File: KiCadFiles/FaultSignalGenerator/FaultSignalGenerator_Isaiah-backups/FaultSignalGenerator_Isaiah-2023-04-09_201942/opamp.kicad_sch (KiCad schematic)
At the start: 16 parts, among them U10 TL074CDR, U11 TL074CDR, U12 TL074CDR, U13 TL074CDR, U5 TL074CDR, U6 TL074CDR, U7 TL074CDR, U8 TL074CDR, U9 TL074CDR

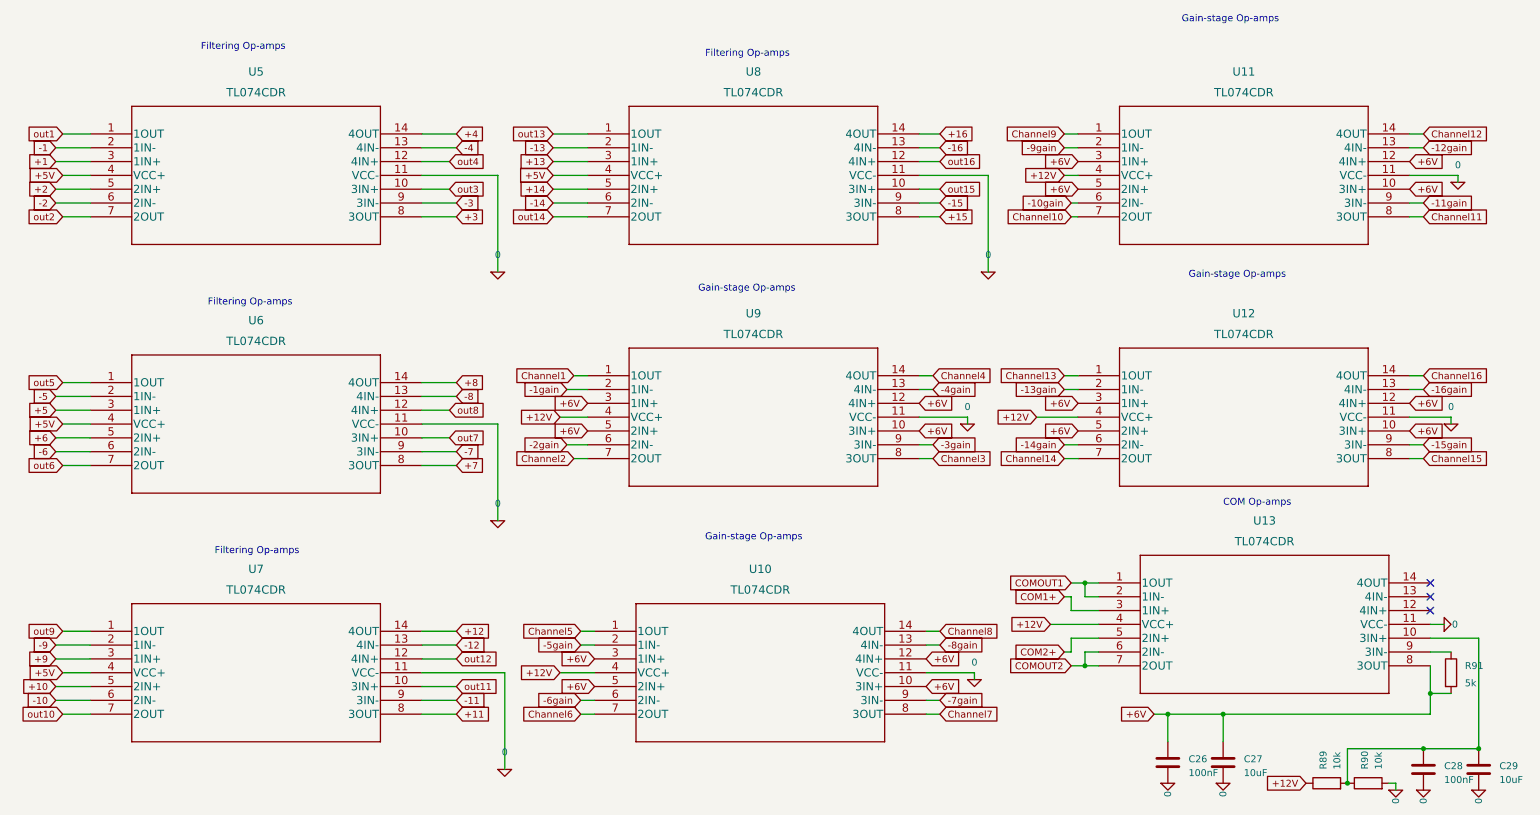
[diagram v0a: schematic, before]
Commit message: Finish schematic, start on PCB
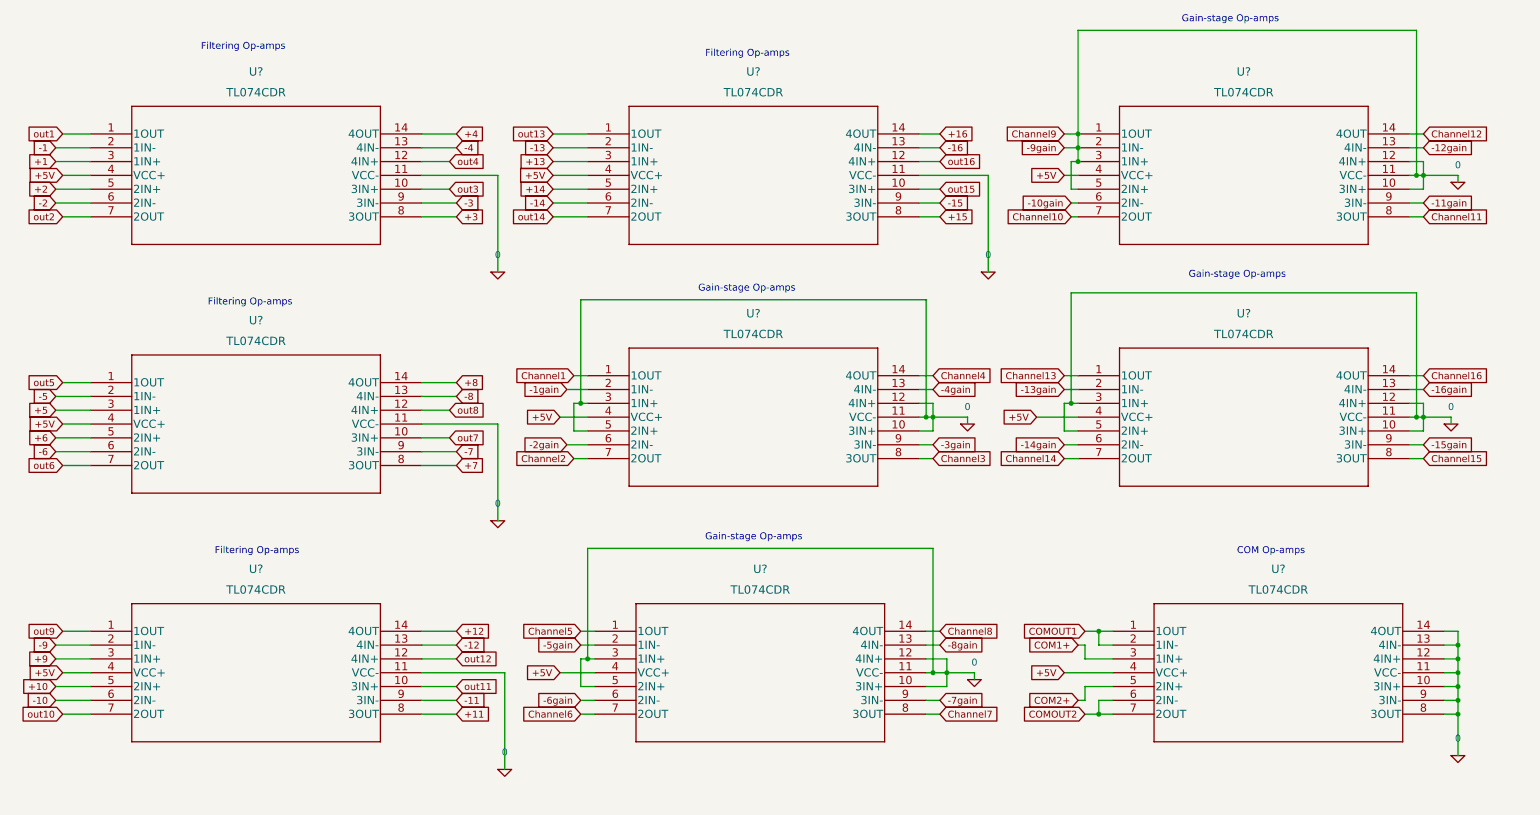
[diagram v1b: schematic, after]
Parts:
- removed C26, C28: 100nF, Capacitor_SMD:C_1206_3216Metric_Pad1.33x1.80mm_HandSolder, symbol Device:C
- removed C27, C29: 10uF, Capacitor_SMD:CP_Elec_4x5.4, symbol Device:C
- removed R89, R90: 10k, Resistor_SMD:R_1206_3216Metric, symbol Device:R
- removed R91: 5k, Resistor_SMD:R_1206_3216Metric, symbol Device:R
- U?: renamed from U12; footprint Package_SO:SOIC-14_3.9x8.7mm_P1.27mm -> TL074CDR_OpAmp:TL074CDR
- U?: renamed from U6; footprint Package_SO:SOIC-14_3.9x8.7mm_P1.27mm -> TL074CDR_OpAmp:TL074CDR
- U?: renamed from U13; footprint Package_SO:SOIC-14_3.9x8.7mm_P1.27mm -> TL074CDR_OpAmp:TL074CDR
- U?: renamed from U11; footprint Package_SO:SOIC-14_3.9x8.7mm_P1.27mm -> TL074CDR_OpAmp:TL074CDR
- U?: renamed from U9; footprint Package_SO:SOIC-14_3.9x8.7mm_P1.27mm -> TL074CDR_OpAmp:TL074CDR
- U?: renamed from U8; footprint Package_SO:SOIC-14_3.9x8.7mm_P1.27mm -> TL074CDR_OpAmp:TL074CDR
- U?: renamed from U10; footprint Package_SO:SOIC-14_3.9x8.7mm_P1.27mm -> TL074CDR_OpAmp:TL074CDR
- U?: renamed from U7; footprint Package_SO:SOIC-14_3.9x8.7mm_P1.27mm -> TL074CDR_OpAmp:TL074CDR
- U?: renamed from U5; footprint Package_SO:SOIC-14_3.9x8.7mm_P1.27mm -> TL074CDR_OpAmp:TL074CDR
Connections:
- net +12V is gone; now on net +5V: U?.4 (VCC+), U?.4 (VCC+), U?.4 (VCC+), U?.4 (VCC+), U?.4 (VCC+)
- net +6V is gone; now on net 0: U?.10 (3IN+), U?.10 (3IN+), U?.10 (3IN+), U?.10 (3IN+), U?.12 (4IN+), U?.12 (4IN+), U?.12 (4IN+), U?.12 (4IN+), U?.3 (1IN+), U?.3 (1IN+), U?.3 (1IN+), U?.3 (1IN+), U?.5 (2IN+), U?.5 (2IN+), U?.5 (2IN+), U?.5 (2IN+), U?.8 (3OUT)
- net -9gain is gone; now on net 0: U?.2 (1IN-)
- net Channel9 is gone; now on net 0: U?.1 (1OUT)
- net 0: now also U?.10 (3IN+), U?.12 (4IN+), U?.13 (4IN-), U?.14 (4OUT), U?.9 (3IN-)
- no-connect marks 3 -> 0
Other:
- moved on the sheet: U?
